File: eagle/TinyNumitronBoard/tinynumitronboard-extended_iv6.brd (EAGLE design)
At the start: 100 x 50 mm, 51 parts, among them IC1 74LS595D

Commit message: IV6 board dev continued.
Before taking some leap on placement. Schematics are ok minus final
review.
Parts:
- removed IC1: 74LS595D, SparkFun-DigitalIC:SO16
- removed J1, J2: (no value), SparkFun-Connectors:1X01NS-KIT
- removed LED2, LED3, LED4: (no value), led:KA-3528ASYC
- removed R10, R11, R12, R13, R14, R15, R16, R17, R18, R19, R20, R21, R22, R23, R24, R25, R26, R27, R28, R29, R30, R31, R32, R9: (no value), resistor:R1206
- removed U$2, U$5, U$7: IV16TINY_NUMITRON, kalshagar:IV16TINY_NUMITRON_PAC
- removed U$4: IV6_NUMITRONLARGE, kalshagar:IV6_NUMITRON_PAC_LARGE
- removed U$6: ULN2803, uln2803:SO18L
- removed UC2, UC3, UC4: 74HC595_SMDDIP_COMBOTHINPAD, kalshagar:DIL16_SO16_PAC2
- added DRIVER1, DRIVER2, DRIVER3, DRIVER4: ULN2803, uln2803:SO18L
- added FILGND2GND: JUMPER-PAD-2-NOYES_SILK, SparkFun-Passives:PAD-JUMPER-2-NO_YES_SILK
- added J_LED_IN, J_LED_OUT: (no value), SparkFun-Connectors:1X01NS-KIT
- added J_TUBEPOWER_IN, J_TUBEPOWER_OUT: (no value), SparkFun-Connectors:1X03_LOCK
- added SER1, SER2, SER3, SER4: 74LS595D, SparkFun-DigitalIC:SO16
- added TUBE1, TUBE2, TUBE3, TUBE4: IV6_NUMITRONLARGE, kalshagar:IV6_NUMITRON_PAC_LARGE
- C1: device resistor:C050-024X044 -> resistor:C1206
- moved D1 31.8 mm to (45.1, 9.53)
- moved JP_INPUT 5.08 mm to (2.54, 12.7)
- moved JP_OUTPUT 5.08 mm to (97.8, 12.7)
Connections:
- removed net N$20: R9.2, U$2.PBL
- removed net N$22: JP_OUTPUT.5, JP_OUTPUT.6, UC4.9, UC4.S9
- removed net N$75: R31.1, UC3.6, UC3.S6
- removed net N$76: R32.1, UC3.7, UC3.S7
- removed net N$77: LED3.A, R32.2, U$7.DOT
- removed net N$78: UC3.9, UC3.S9, UC4.14, UC4.S14
- new net FIL_M: FILGND2GND.1, J_TUBEPOWER_IN.3, J_TUBEPOWER_OUT.3, TUBE1.FIL_M, TUBE2.FIL_M, TUBE3.FIL_M, TUBE4.FIL_M
- new net FIL_P: J_TUBEPOWER_IN.2, J_TUBEPOWER_OUT.2, TUBE1.FIL_P, TUBE2.FIL_P, TUBE3.FIL_P, TUBE4.FIL_P
- new net GRID_P: J_TUBEPOWER_IN.1, J_TUBEPOWER_OUT.1, TUBE1.GRID_P, TUBE2.GRID_P, TUBE3.GRID_P, TUBE4.GRID_P
- new net N$13: SER2.9, SER3.14
- new net N$14: DRIVER2.18, TUBE2.BL
- new net N$16: DRIVER2.17, TUBE2.BOT
- new net N$17: DRIVER2.16, TUBE2.MID
- new net N$60: DRIVER3.16, TUBE3.MID
- new net N$61: DRIVER3.15, TUBE3.TL
- net GND: now also DRIVER1.9, DRIVER2.9, DRIVER3.9, DRIVER4.9, FILGND2GND.2, SER1.13, SER1.8, SER2.13, SER2.8, SER3.13, SER3.8, SER4.13, SER4.8; no longer IC1.13, IC1.8, LED2.C, LED3.C, LED4.C, U$6.9, UC2.13, UC2.8, UC2.S13, UC2.S8, UC3.13, UC3.8, UC3.S13, UC3.S8, UC4.13, UC4.8, UC4.S13, UC4.S8
- net N$1: now also DRIVER1.1, SER1.15; no longer IC1.15, U$6.1
- net N$12: now also J_LED_IN.1; no longer J1.1
- net N$15: now also DRIVER1.18, TUBE1.BL; no longer U$4.BL, U$6.18
- net N$18: now also DRIVER1.17, TUBE1.BOT; no longer U$4.BOT, U$6.17
- net N$19: now also DRIVER1.16, TUBE1.MID; no longer U$4.MID, U$6.16
- net N$2: now also DRIVER1.2, SER1.1; no longer IC1.1, U$6.2
- net N$21: now also JP_OUTPUT.5, JP_OUTPUT.6, SER4.9; no longer R10.2, U$2.PB
- net N$23: now also SER1.9, SER2.14; no longer IC1.9, UC2.14, UC2.S14
- net N$24: now also DRIVER4.18, TUBE4.BL; no longer R11.2, U$2.PM
- net N$25: now also DRIVER4.17, TUBE4.BOT; no longer R12.2, U$2.PTL
- net N$26: now also DRIVER4.16, TUBE4.MID; no longer R13.2, U$2.PT
- net N$27: now also DRIVER4.15, TUBE4.TL; no longer R14.2, U$2.PBR
- net N$28: now also DRIVER4.14, TUBE4.TOP; no longer R15.2, U$2.PTR
- net N$29: now also DRIVER4.13, TUBE4.BR; no longer R9.1, UC4.15, UC4.S15
- net N$3: now also DRIVER1.3, SER1.2; no longer IC1.2, U$6.3
- net N$30: now also DRIVER4.12, TUBE4.TR; no longer R10.1, UC4.1, UC4.S1
- net N$31: now also DRIVER4.11, TUBE4.DOT; no longer R11.1, UC4.2, UC4.S2
- net N$32: now also DRIVER4.1, SER4.15; no longer R12.1, UC4.3, UC4.S3
- net N$33: now also DRIVER4.2, SER4.1; no longer R13.1, UC4.4, UC4.S4
- net N$34: now also DRIVER4.3, SER4.2; no longer R14.1, UC4.5, UC4.S5
- net N$35: now also DRIVER4.4, SER4.3; no longer R15.1, UC4.6, UC4.S6
- net N$36: now also DRIVER4.5, SER4.4; no longer R16.1, UC4.7, UC4.S7
- net N$37: now also DRIVER4.6, SER4.5; no longer LED4.A, R16.2, U$2.DOT
- net N$38: now also DRIVER1.15, TUBE1.TL; no longer U$4.TL, U$6.15
- net N$39: now also DRIVER2.15, TUBE2.TL; no longer R17.2, U$5.PBL
- net N$4: now also DRIVER1.4, SER1.3; no longer IC1.3, U$6.4
- net N$40: now also DRIVER2.14, TUBE2.TOP; no longer R18.2, U$5.PB
- net N$41: now also DRIVER2.13, TUBE2.BR; no longer R19.2, U$5.PM
- net N$42: now also DRIVER2.12, TUBE2.TR; no longer R20.2, U$5.PTL
- net N$43: now also DRIVER2.11, TUBE2.DOT; no longer R21.2, U$5.PT
- net N$44: now also DRIVER2.1, SER2.15; no longer R22.2, U$5.PBR
- net N$45: now also DRIVER2.2, SER2.1; no longer R23.2, U$5.PTR
- net N$46: now also DRIVER2.3, SER2.2; no longer R17.1, UC2.15, UC2.S15
- net N$47: now also DRIVER2.4, SER2.3; no longer R18.1, UC2.1, UC2.S1
- net N$48: now also DRIVER2.5, SER2.4; no longer R19.1, UC2.2, UC2.S2
- net N$49: now also DRIVER2.6, SER2.5; no longer R20.1, UC2.3, UC2.S3
- net N$5: now also DRIVER1.5, SER1.4; no longer IC1.4, U$6.5
- net N$50: now also DRIVER2.7, SER2.6; no longer R21.1, UC2.4, UC2.S4
- net N$51: now also DRIVER2.8, SER2.7; no longer R22.1, UC2.5, UC2.S5
- net N$52: now also DRIVER4.7, SER4.6; no longer R23.1, UC2.6, UC2.S6
- net N$53: now also SER3.9, SER4.14; no longer R24.1, UC2.7, UC2.S7
- net N$54: now also DRIVER3.18, TUBE3.BL; no longer LED2.A, R24.2, U$5.DOT
- net N$55: now also DRIVER1.14, TUBE1.TOP; no longer U$4.TOP, U$6.14
- net N$56: now also DRIVER1.13, TUBE1.BR; no longer U$4.BR, U$6.13
- net N$57: now also DRIVER1.12, TUBE1.TR; no longer U$4.TR, U$6.12
- net N$58: now also DRIVER3.17, TUBE3.BOT; no longer UC2.9, UC2.S9, UC3.14, UC3.S14
- net N$59: now also DRIVER1.11, TUBE1.DOT; no longer U$4.DOT, U$6.11
- net N$6: now also DRIVER1.6, SER1.5; no longer IC1.5, U$6.6
- net N$62: now also DRIVER3.14, TUBE3.TOP; no longer R25.2, U$7.PBL
- net N$63: now also DRIVER3.13, TUBE3.BR; no longer R26.2, U$7.PB
- net N$64: now also DRIVER3.12, TUBE3.TR; no longer R27.2, U$7.PM
- net N$65: now also DRIVER3.11, TUBE3.DOT; no longer R28.2, U$7.PTL
- net N$66: now also DRIVER3.1, SER3.15; no longer R29.2, U$7.PT
- net N$67: now also DRIVER3.2, SER3.1; no longer R30.2, U$7.PBR
- net N$68: now also DRIVER3.3, SER3.2; no longer R31.2, U$7.PTR
- net N$69: now also DRIVER3.4, SER3.3; no longer R25.1, UC3.15, UC3.S15
- net N$7: now also DRIVER1.7, SER1.6; no longer IC1.6, U$6.7
- net N$70: now also DRIVER3.5, SER3.4; no longer R26.1, UC3.1, UC3.S1
- net N$71: now also DRIVER3.6, SER3.5; no longer R27.1, UC3.2, UC3.S2
- net N$72: now also DRIVER3.7, SER3.6; no longer R28.1, UC3.3, UC3.S3
- net N$73: now also DRIVER3.8, SER3.7; no longer R29.1, UC3.4, UC3.S4
- net N$74: now also DRIVER4.8, SER4.7; no longer R30.1, UC3.5, UC3.S5
- net N$8: now also DRIVER1.8, SER1.7; no longer IC1.7, U$6.8
- net RCK: now also SER1.12, SER2.12, SER3.12, SER4.12; no longer IC1.12, UC2.12, UC2.S12, UC3.12, UC3.S12, UC4.12, UC4.S12
- net SCK: now also SER1.11, SER2.11, SER3.11, SER4.11; no longer IC1.11, UC2.11, UC2.S11, UC3.11, UC3.S11, UC4.11, UC4.S11
- net SER: now also SER1.14; no longer IC1.14
- net VCC: now also J_LED_OUT.1, SER1.10, SER1.16, SER2.10, SER2.16, SER3.10, SER3.16, SER4.10, SER4.16; no longer IC1.10, IC1.16, J2.1, U$2.VCC, U$5.VCC, U$7.VCC, UC2.10, UC2.16, UC2.S10, UC2.S16, UC3.10, UC3.16, UC3.S10, UC3.S16, UC4.10, UC4.16, UC4.S10, UC4.S16
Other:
- board text removed: "1uF"
- board text removed: "74xx595"
- board text removed: "Dot/LED"

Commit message: Layout first draft finished.
Todo review.
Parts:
- moved SER4 165.6 mm to (64.8, 11.4), flipped to the bottom
- moved SER3 163.7 mm to (85.1, 38.1), flipped to the bottom, turned to 180 degrees
- moved DRIVER4 163.1 mm to (85.1, 10.2), flipped to the bottom
- moved DRIVER3 146.2 mm to (64.8, 39.4), flipped to the bottom, turned to 180 degrees
- moved D4 95.3 mm to (85.0, 25.0), turned to 180 degrees
- moved SER2 77.8 mm to (14.0, 10.2), flipped to the bottom
- moved D3 75.0 mm to (65.0, 25.0), turned to 180 degrees
- moved DRIVER2 71.2 mm to (34.3, 8.89), flipped to the bottom
- moved C2 71.2 mm to (50.0, 25.0), flipped to the bottom, turned to 90 degrees
- moved D2 47.9 mm to (35.0, 25.0), turned to 180 degrees
- moved D1 33.8 mm to (15.0, 25.0)
- moved C1 22.5 mm to (39.8, 44.9), turned to 90 degrees
- moved SER1 16.1 mm to (29.2, 38.1), turned to 180 degrees
- moved DRIVER1 10.5 mm to (15.2, 39.4), turned to 180 degrees
- moved TUBE1 2.50 mm to (15.0, 25.0)
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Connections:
- new net N$20: D4.2, J_LED_OUT.1
- net VCC: no longer J_LED_OUT.1

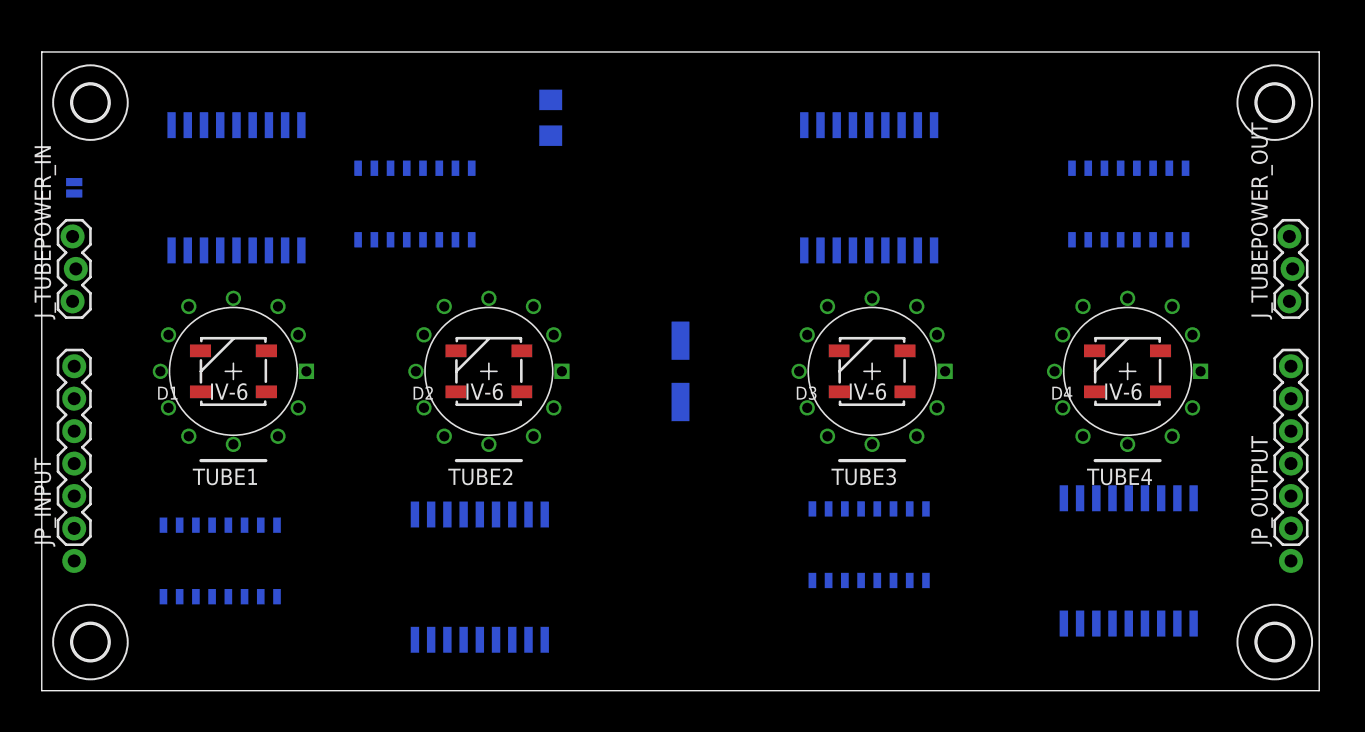
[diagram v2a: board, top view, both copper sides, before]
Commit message: Added options for 2 led in the middle
And a solder jumper for the dot or not (default not)
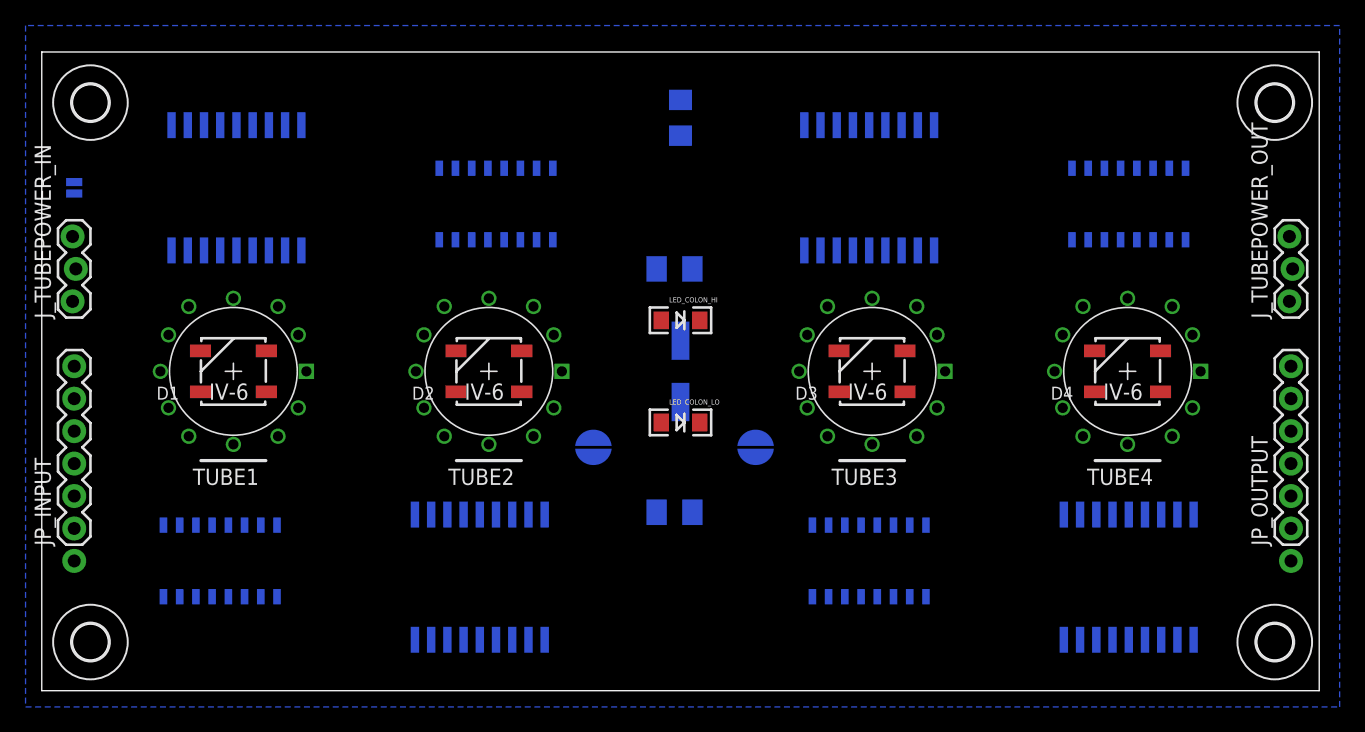
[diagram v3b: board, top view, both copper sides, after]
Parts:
- added JP_DOT_TUBE2, JP_DOT_TUBE3: JUMPER-PAD-2-NOROUND, SparkFun-Passives:PAD-JUMPER-2-NO_YES_SILK_ROUND
- added LED_COLON_HI, LED_COLON_LO: (no value), SparkFun-LED:LED-1206
- added R_COLON_HI, R_COLON_LO: 470, resistor:M1206
- moved C1 10.2 mm to (50.0, 44.9)
- moved SER1 6.35 mm to (35.6, 38.1)
- moved DRIVER4 1.27 mm to (85.1, 8.89)
- moved SER4 1.27 mm to (64.8, 10.2)
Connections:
- new net N$22: LED_COLON_LO.C, R_COLON_LO.2
- new net N$75: JP_DOT_TUBE2.2, TUBE2.DOT
- new net N$76: JP_DOT_TUBE3.2, TUBE3.DOT
- new net N$77: LED_COLON_HI.C, R_COLON_HI.2
- net N$43: now also JP_DOT_TUBE2.1, R_COLON_LO.1; no longer TUBE2.DOT
- net N$65: now also JP_DOT_TUBE3.1, R_COLON_HI.1; no longer TUBE3.DOT
- net VCC: now also LED_COLON_HI.A, LED_COLON_LO.A
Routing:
- added copper zone on layer 16, net GND

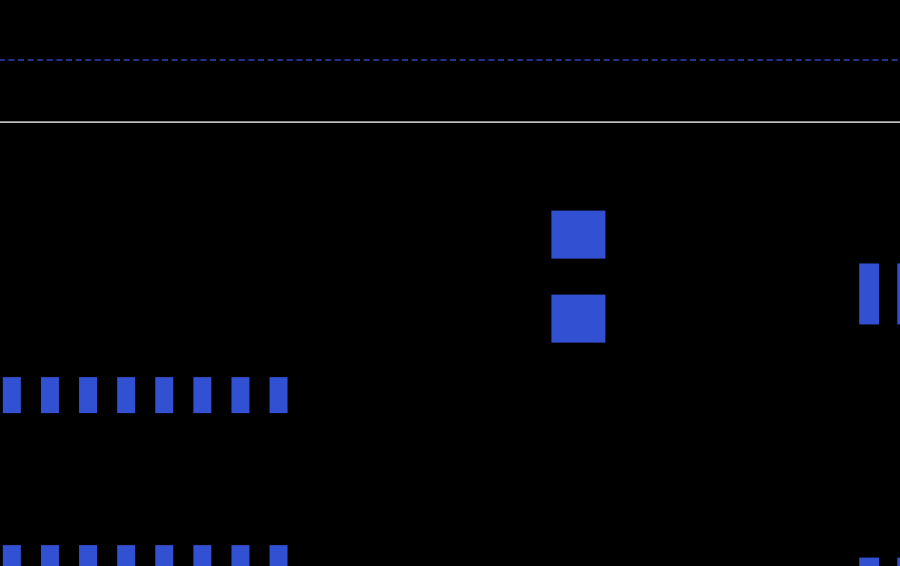
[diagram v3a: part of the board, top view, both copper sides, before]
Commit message: added pad for UL2803 diode/common
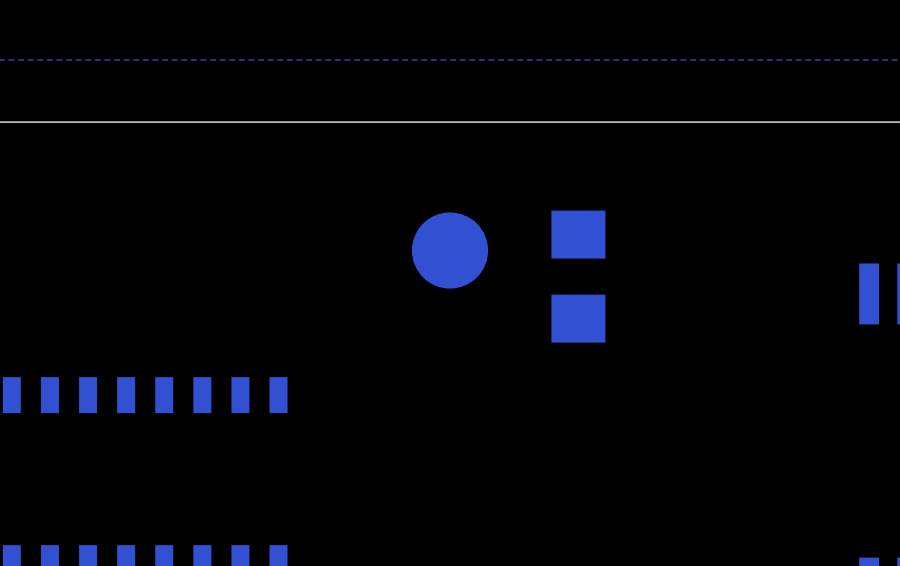
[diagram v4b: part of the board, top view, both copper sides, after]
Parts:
- added TP1: TPB2,54, testpad:B2,54
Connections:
- new net DIODE: DRIVER1.10, TP1.TP
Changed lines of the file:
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@@
 <element name="R_COLON_HI" library="resistor" package="M1206" value="470" x="49.53" y="33.02" rot="MR0"/>
 <element name="JP_DOT_TUBE3" library="SparkFun-Passives" package="PAD-JUMPER-2-NO_YES_SILK_ROUND" value="JUMPER-PAD-2-NOROUND" x="55.88" y="19.05" rot="MR90"/>
+<element name="TP1" library="testpad" package="B2,54" value="TPB2,54" x="45.72" y="45.72" rot="MR0">
+<attribute name="TP_SIGNAL_NAME" value="" x="45.72" y="45.72" size="1.016" layer="28" rot="MR0" display="off"/>
+</element>
 </elements>
 <signals>
@@
 <wire x1="84.455" y1="35.3" x2="82.423" y2="26.6" width="0" layer="19" extent="1-16"/>
 <wire x1="32.423" y1="26.6" x2="34.925" y2="35.3" width="0" layer="19" extent="1-16"/>
-<wire x1="62.423" y1="26.6" x2="65.405" y2="12.96" width="0" layer="19" extent="1-16"/>
+<wire x1="62.423" y1="26.6" x2="50" y2="22.6" width="0" layer="19" extent="1-16"/>
 <wire x1="12.423" y1="26.6" x2="14.605" y2="12.96" width="0" layer="19" extent="1-16"/>
 </signal>
@@
 <wire x1="48.5" y1="21" x2="61.595" y2="12.96" width="0" layer="19" extent="1-16"/>
 <wire x1="50" y1="27.4" x2="48.5" y2="21" width="0" layer="19" extent="1-16"/>
+<wire x1="48.5" y1="29" x2="50" y2="27.4" width="0" layer="19" extent="1-16"/>
 <wire x1="37.577" y1="23.4" x2="48.5" y2="21" width="0" layer="19" extent="1-1"/>
-<wire x1="38.735" y1="35.3" x2="37.577" y2="23.4" width="0" layer="19" extent="1-16"/>
+<wire x1="38.735" y1="35.3" x2="48.5" y2="29" width="0" layer="19" extent="1-16"/>
 <wire x1="31.115" y1="35.3" x2="38.735" y2="35.3" width="0" layer="19" extent="16-16"/>
 <wire x1="17.577" y1="23.4" x2="31.115" y2="35.3" width="0" layer="19" extent="1-16"/>
@@
 <wire x1="10.795" y1="12.96" x2="18.415" y2="12.96" width="0" layer="19" extent="16-16"/>
 <wire x1="2.54" y1="15.24" x2="10.795" y2="12.96" width="0" layer="19" extent="16-16"/>
-<wire x1="48.5" y1="29" x2="2.54" y2="15.24" width="0" layer="19" extent="1-1"/>
 </signal>
 <signal name="SER">
@@
 <contactref element="R_COLON_LO" pad="1"/>
 <contactref element="JP_DOT_TUBE2" pad="1"/>
-<wire x1="48.13" y1="13.97" x2="30.48" y2="13.7922" width="0" layer="19" extent="1-16"/>
-<wire x1="43.18" y1="17.78" x2="48.13" y2="13.97" width="0" layer="19" extent="1-1"/>
+<wire x1="48.13" y1="13.97" x2="43.18" y2="17.78" width="0" layer="19" extent="16-16"/>
+<wire x1="30.48" y1="13.7922" x2="43.18" y2="17.78" width="0" layer="19" extent="16-16"/>
 </signal>
 <signal name="N$44">
@@
 <contactref element="R_COLON_HI" pad="1"/>
 <contactref element="JP_DOT_TUBE3" pad="1"/>
-<wire x1="50.93" y1="33.02" x2="68.58" y2="34.4678" width="0" layer="19" extent="1-16"/>
-<wire x1="55.88" y1="17.78" x2="50.93" y2="33.02" width="0" layer="19" extent="1-1"/>
+<wire x1="50.93" y1="33.02" x2="68.58" y2="34.4678" width="0" layer="19" extent="16-16"/>
+<wire x1="55.88" y1="17.78" x2="50.93" y2="33.02" width="0" layer="19" extent="16-16"/>
 </signal>
 <signal name="N$66">
@@
 <contactref element="R_COLON_LO" pad="2"/>
 <contactref element="LED_COLON_LO" pad="C"/>
-<wire x1="51.5" y1="21" x2="50.93" y2="13.97" width="0" layer="19" extent="1-1"/>
+<wire x1="50.93" y1="13.97" x2="51.5" y2="21" width="0" layer="19" extent="1-16"/>
 </signal>
 <signal name="N$75">
 <contactref element="JP_DOT_TUBE2" pad="2"/>
 <contactref element="TUBE2" pad="DOT"/>
-<wire x1="43.18" y1="20.32" x2="40.08" y2="22.1425" width="0" layer="19" extent="1-1"/>
+<wire x1="40.08" y1="22.1425" x2="43.18" y2="20.32" width="0" layer="19" extent="16-16"/>
 </signal>
 <signal name="N$77">
 <contactref element="R_COLON_HI" pad="2"/>
 <contactref element="LED_COLON_HI" pad="C"/>
-<wire x1="48.13" y1="33.02" x2="51.5" y2="29" width="0" layer="19" extent="1-1"/>
+<wire x1="51.5" y1="29" x2="48.13" y2="33.02" width="0" layer="19" extent="1-16"/>
 </signal>
 <signal name="N$76">
 <contactref element="JP_DOT_TUBE3" pad="2"/>
 <contactref element="TUBE3" pad="DOT"/>
-<wire x1="55.88" y1="20.32" x2="70.08" y2="22.1425" width="0" layer="19" extent="1-1"/>
+<wire x1="55.88" y1="20.32" x2="70.08" y2="22.1425" width="0" layer="19" extent="16-16"/>
+</signal>
+<signal name="DIODE">
+<contactref element="DRIVER1" pad="10"/>
+<contactref element="TP1" pad="TP"/>
+<wire x1="20.32" y1="34.4678" x2="45.72" y2="45.72" width="0" layer="19" extent="16-16"/>
 </signal>
 </signals>

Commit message: Routing finished, need some art and final review
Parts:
- moved TP1 25.4 mm to (25.4, 30.5)
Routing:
- net VCC: track 0.00 -> 254.1 mm, vias 0 -> 5
- net FIL_M: track 0.00 -> 204.9 mm
- net RCK: track 0.00 -> 201.9 mm, vias 0 -> 4
- net SCK: track 0.00 -> 187.2 mm, vias 0 -> 6
- net N$13: track 0.00 -> 154.2 mm, vias 0 -> 2
- net FIL_P: track 0.00 -> 133.1 mm
- net GRID_P: track 0.00 -> 117.2 mm, vias 0 -> 3
- net N$21: track 0.00 -> 45.8 mm, vias 0 -> 1
- net N$23: track 0.00 -> 45.3 mm, vias 0 -> 2
- net N$53: track 0.00 -> 39.8 mm, vias 0 -> 2
- net SER: track 0.00 -> 38.5 mm, vias 0 -> 1
- net N$65: track 0.00 -> 38.2 mm
- net N$10: track 0.00 -> 34.7 mm, vias 0 -> 2
- net N$32: track 0.00 -> 31.3 mm
- net N$30: track 0.00 -> 30.4 mm
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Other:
- board text added: "http://electrogeek.cc/Alan numitron clock.html"
- board text removed: "http://electrogeek.cc/Alan+numitron+clock"

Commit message: Still optimizing/reviewing
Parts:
- JP_DOT_TUBE2, JP_DOT_TUBE3: value JUMPER-PAD-2-NOROUND -> JUMPER-PAD-2-NOYES_SILK; device SparkFun-Passives:PAD-JUMPER-2-NO_YES_SILK_ROUND -> SparkFun-Passives:PAD-JUMPER-2-NO_YES_SILK
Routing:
- net N$14: track 26.0 -> 30.4 mm
- net N$16: track 20.0 -> 23.0 mm
- net VCC: track 254.1 -> 255.9 mm
- net N$10: track 34.7 -> 36.4 mm
- net N$65: track 38.2 -> 39.6 mm
- net N$77: track 5.47 -> 6.85 mm
- net SCK: track 187.2 -> 188.6 mm
- net N$75: track 4.03 -> 5.11 mm
- net N$43: track 24.0 -> 24.7 mm
- net N$27: track 19.2 -> 19.9 mm
- net N$37: track 28.7 -> 29.5 mm
- net N$59: track 14.3 -> 15.0 mm
- net N$63: track 21.1 -> 21.6 mm

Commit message: Still reviewing
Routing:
- net N$23: track 45.3 -> 47.9 mm
- net VCC: track 255.9 -> 258.2 mm
- net N$43: track 24.7 -> 25.8 mm
- net RCK: track 201.9 -> 202.9 mm
- net N$70: track 23.4 -> 24.0 mm
- net GND: track 7.37 -> 8.03 mm
- net N$27: track 19.9 -> 20.5 mm
